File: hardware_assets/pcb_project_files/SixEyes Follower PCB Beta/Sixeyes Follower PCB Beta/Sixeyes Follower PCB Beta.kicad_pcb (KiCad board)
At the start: 2 copper layers, 9 parts, among them J1 Micro_SD_Card, J12 Conn_01x02_Pin, U1 ESP32-S3-WROOM-1, U2 TMC2209-LA, U3 TMC2209-LA, U4 TMC2209-LA, U5 TMC2209-LA, U6 MIC5219-3.3YM5, U7 CH340K

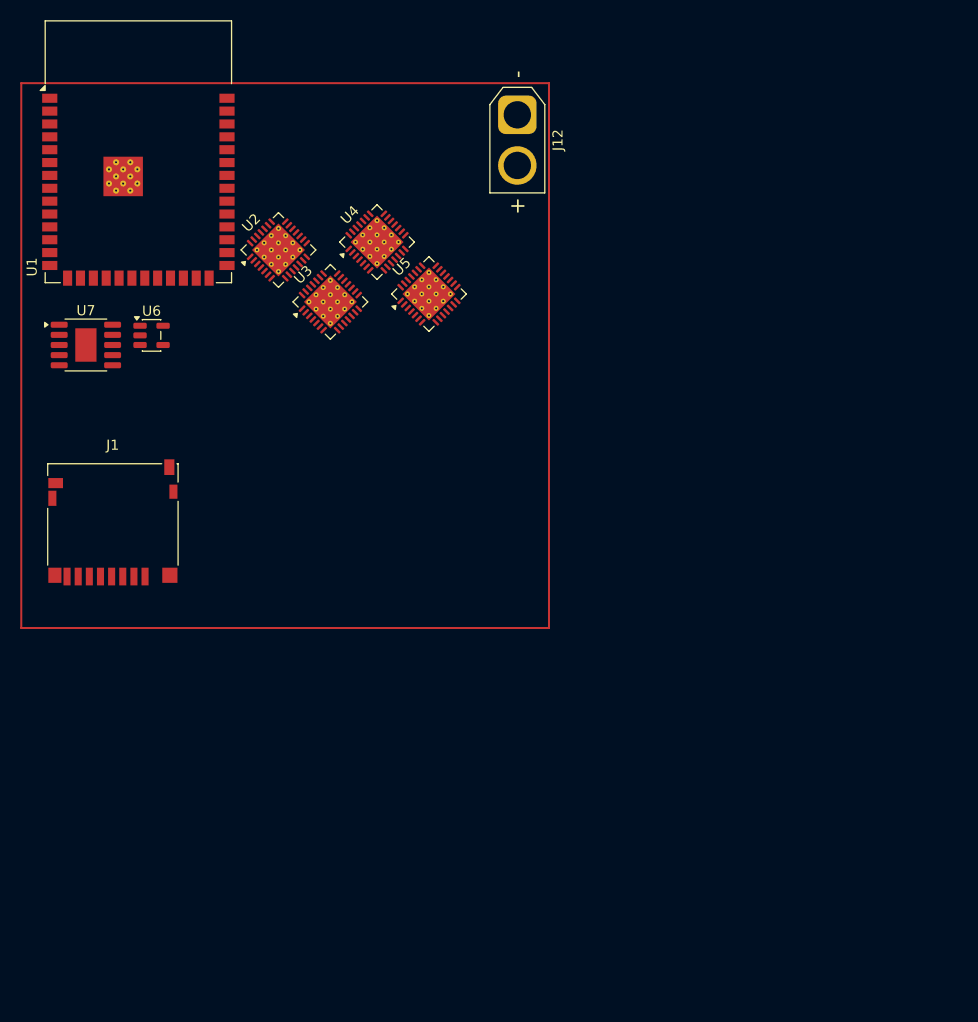
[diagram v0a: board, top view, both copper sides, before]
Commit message: feat: add Beta PCB schematic symbols, 3D models, custom footprints; update README
Schematic (Sixeyes Follower PCB Beta.kicad_sch):
- Add TPS54540B (6.6V sync buck) symbol and instance U8
- Add LMR14030S (5.0V async buck) symbol and instance U9
- Add USB_C_Receptacle_USB2.0 symbols for J13 (J_USB1, native OTG) and J14 (J_USB2, CH340K)
- Add Conn_01x02_Pin instance J15 (J_LDR_PWR, Node1 5V/GND power, separate from J6 signals)
- All symbols reference correct footprints and datasheets per Beta Rev2 design spec

Hardware assets:
- Add 3D models: TMC2209, TPS54540B, LMR14030S, USB-C, XT30, Molex 2/3/4-pin
- Add CustomFootprints.pretty with sanka.kicad_mod and sanka2.kicad_mod
- Add docs/references/Sixeyes Node0 (Folloer PCB Beta).txt (Beta Rev2 design spec)

README.md:
- Fix GitHub org (SixEyes-Open-Source → studiosanka)
- Fix firmware structure to show alpha/beta split
- Fix hardware_assets paths (pcb_project_files, pcb_latest_gerber)
- Add Alpha vs Beta hardware generation comparison table
- Update build commands to target firmware/alpha and firmware/beta
- Add Beta PCB to Project Status
- Update Last Updated to June 2026

Co-Authored-By: Claude Sonnet 4.6 <noreply@anthropic.com>
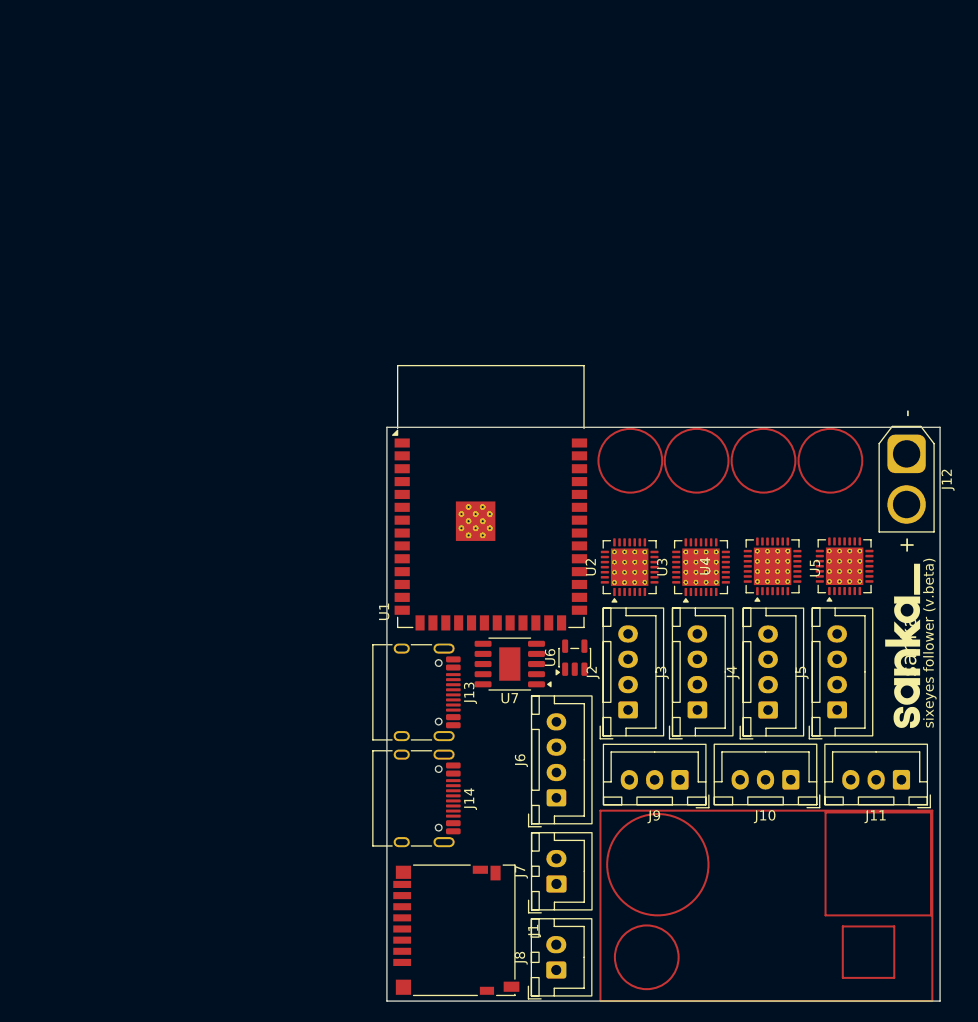
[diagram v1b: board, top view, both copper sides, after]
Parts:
- added J10: Conn_01x03_Pin, Connector_JST:JST_XH_B3B-XH-A_1x03_P2.50mm_Vertical, F.Cu at (156.0, 114.0)
- added J11: Conn_01x03_Pin, Connector_JST:JST_XH_B3B-XH-A_1x03_P2.50mm_Vertical, F.Cu at (166.9, 114.0)
- added J13: USB_C_Receptacle_USB2.0, Connector_USB:USB_C_Receptacle_HRO_TYPE-C-31-M-12, F.Cu at (118.6, 105.4)
- added J14: USB_C_Receptacle_USB2.0, Connector_USB:USB_C_Receptacle_HRO_TYPE-C-31-M-12, F.Cu at (118.6, 115.9)
- added J2: Conn_01x04_Pin, Connector_JST:JST_XH_B4B-XH-A_1x04_P2.50mm_Vertical, F.Cu at (139.9, 107.1)
- added J3: Conn_01x04_Pin, Connector_JST:JST_XH_B4B-XH-A_1x04_P2.50mm_Vertical, F.Cu at (146.7, 107.1)
- added J4: Conn_01x04_Pin, Connector_JST:JST_XH_B4B-XH-A_1x04_P2.50mm_Vertical, F.Cu at (153.7, 107.2)
- added J5: Conn_01x04_Pin, Connector_JST:JST_XH_B4B-XH-A_1x04_P2.50mm_Vertical, F.Cu at (160.5, 107.1)
- added J6: Conn_01x04_Pin, Connector_JST:JST_XH_B4B-XH-A_1x04_P2.50mm_Vertical, F.Cu at (132.8, 115.8)
- added J7: Conn_01x02_Pin, Connector_JST:JST_XH_B2B-XH-A_1x02_P2.50mm_Vertical, F.Cu at (132.8, 124.3)
- added J8: Conn_01x02_Pin, Connector_JST:JST_XH_B2B-XH-A_1x02_P2.50mm_Vertical, F.Cu at (132.8, 132.8)
- added J9: Conn_01x03_Pin, Connector_JST:JST_XH_B3B-XH-A_1x03_P2.50mm_Vertical, F.Cu at (145.0, 114.1)
- added sanka: LOGO, CustomFootprints:sanka2, F.Cu at (167.6, 100.8)
- moved J1 52.6 mm to (122.9, 128.9), turned to -90 degrees
- moved U6 52.5 mm to (134.6, 102.0), turned to 90 degrees
- moved U7 52.4 mm to (128.2, 102.6), turned to 180 degrees
- moved J12 51.0 mm to (167.4, 81.9)
- moved U4 50.5 mm to (154.2, 93.0), turned to 90 degrees
- moved U5 49.1 mm to (161.3, 93.0), turned to 90 degrees
- moved U1 48.7 mm to (126.3, 86.1)
- moved U2 46.7 mm to (140.0, 93.1), turned to 90 degrees
- moved U3 45.0 mm to (147.1, 93.1), turned to 90 degrees
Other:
- board outline added: 54.6 x 56.6 mm
- board text added: "sixeyes follower (v.beta)"
